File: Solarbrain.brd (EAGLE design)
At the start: 42.9 x 30.4 mm, 51 parts, among them IC1 MCP73871, Q1 MOSFET-NCHANNELSMD, Q2 MOSFET-NCHANNELFDD8580, Q3 MOSFET-NCHANNELSMD, U1 ATMEGA128_SMD

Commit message: fixed a broken connection, clarification on schematic
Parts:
- D1: value (none) -> 1amp
- D3: value (none) -> 3amp
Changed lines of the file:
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@@
 </element>
 <element name="Q2" library="SparkFun2011" package="DPAK" value="MOSFET-NCHANNELFDD8580" x="36.004246875" y="23.721315625" smashed="yes" rot="R270"/>
-<element name="D3" library="SparkFun2011" package="SMA-DIODE" value="" x="8.42645" y="22.02815" smashed="yes" rot="R270">
+<element name="D3" library="SparkFun2011" package="SMA-DIODE" value="3amp" x="8.42645" y="22.02815" smashed="yes" rot="R270">
 <attribute name="NAME" x="10.07745" y="24.31415" size="0.6096" layer="25" rot="R270"/>
 <attribute name="VALUE" x="10.07745" y="21.77415" size="0.4064" layer="27" rot="R270"/>
@@
 <attribute name="VALUE" x="17.937225" y="15.71675625" size="1.27" layer="27" rot="R180"/>
 </element>
-<element name="D1" library="SparkFun2011" package="SMA-DIODE" value="" x="37.4015" y="18.8595" smashed="yes" rot="R180">
+<element name="D1" library="SparkFun2011" package="SMA-DIODE" value="1amp" x="37.4015" y="18.8595" smashed="yes" rot="R180">
 <attribute name="NAME" x="39.6875" y="17.2085" size="0.6096" layer="25" rot="R180"/>
 <attribute name="VALUE" x="37.1475" y="17.2085" size="0.4064" layer="27" rot="R180"/>
@@
 <contactref element="JP3" pad="11"/>
 <contactref element="JP8" pad="5"/>
-<contactref element="JP1" pad="1"/>
 <wire x1="9.271" y1="25.7302" x2="9.478884375" y2="25.7716" width="0.254" layer="1"/>
 <wire x1="8.7214" y1="14.0622" x2="7.80415625" y2="14.0622" width="0.1778" layer="1"/>
@@
 <wire x1="23.845909375" y1="23.951871875" x2="23.82886875" y2="23.68083125" width="0.2032" layer="1"/>
 <wire x1="21.39475" y1="21.397" x2="21.363" y2="23.087" width="0.2032" layer="1"/>
-<wire x1="21.363" y1="23.087" x2="21.2725" y2="23.1775" width="0.2032" layer="1"/>
 <wire x1="18.152228125" y1="15.84325" x2="18.51025" y2="15.875" width="0.2032" layer="1"/>
 <via x="18.51025" y="15.875" extent="1-16" drill="0.8"/>
@@
 <wire x1="26.3525" y1="4.532375" x2="26.360375" y2="4.54025" width="0.6096" layer="1"/>
 <wire x1="26.360375" y1="4.54025" x2="26.416" y2="4.54025" width="0.6096" layer="1"/>
+<contactref element="JP1" pad="1"/>
+<wire x1="21.363" y1="23.087" x2="21.2725" y2="23.087" width="0.4064" layer="1"/>
+<wire x1="21.2725" y1="23.087" x2="21.2725" y2="23.1775" width="0.4064" layer="1"/>
 </signal>
 <signal name="VCC" class="1">

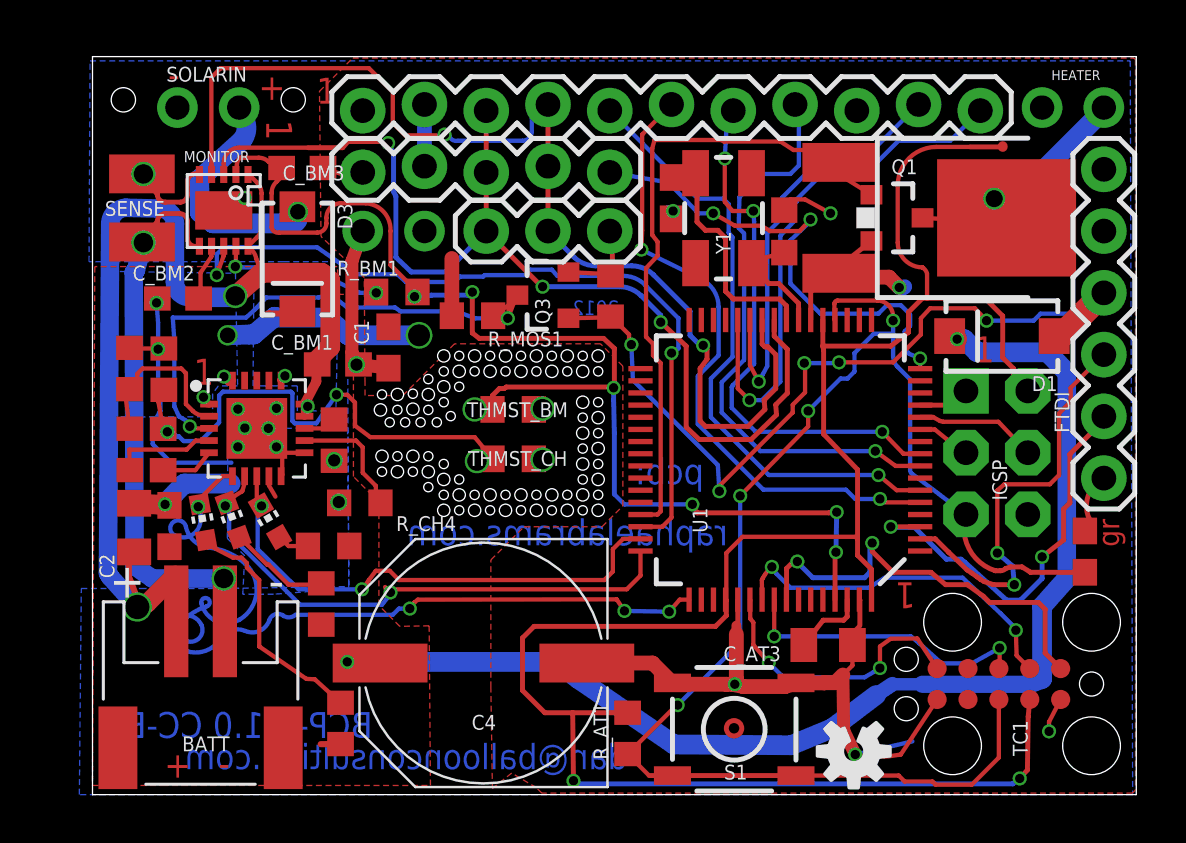
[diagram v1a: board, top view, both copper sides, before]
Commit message: minor tweaks on board, added a via to get to an extra IO pin (pa1)
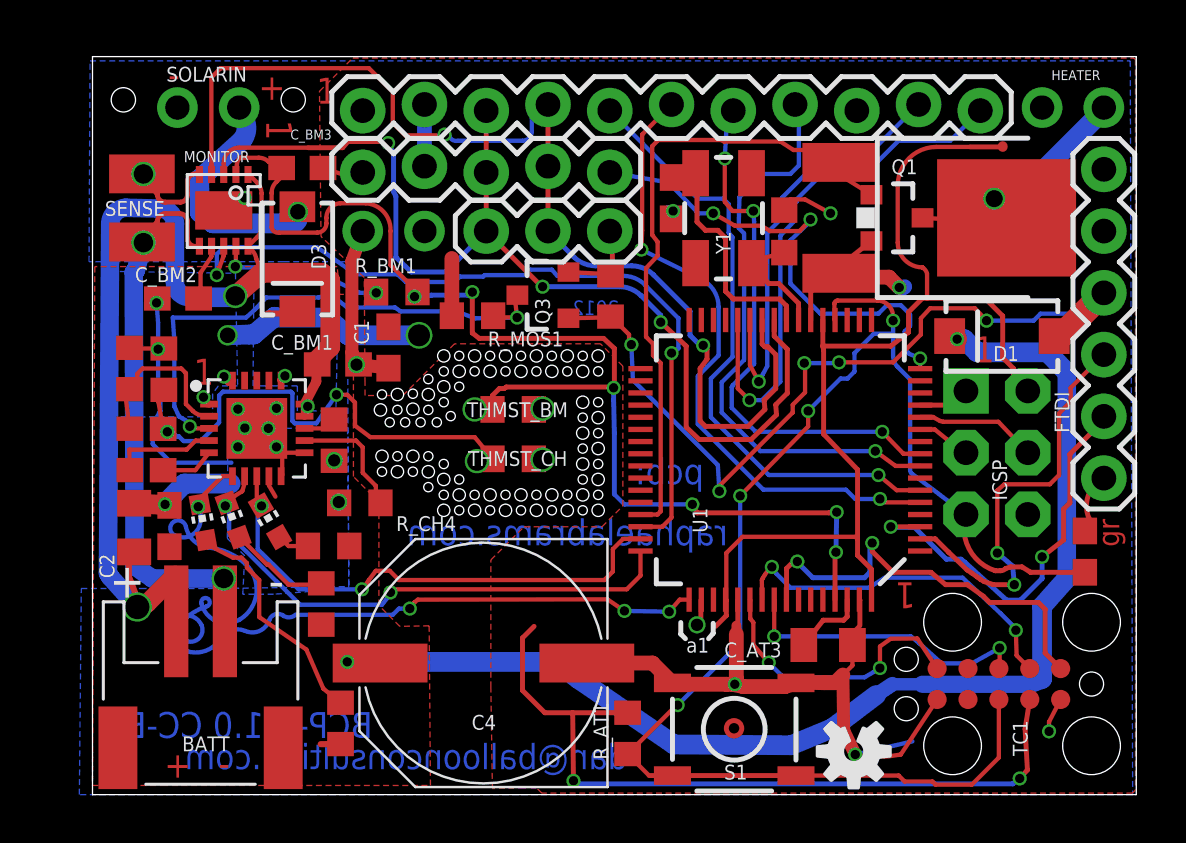
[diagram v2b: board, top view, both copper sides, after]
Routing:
- net 3.3V: track 97.9 -> 90.4 mm
- net N$1: track 0.00 -> 1.03 mm
- net STAT2: track 23.7 -> 23.1 mm
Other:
- board text added: "a1"

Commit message: major tweak list
issues addressed:

  * Atmega Circuit

   1. PWR_EN from sat connector net not connected to any I/O pin on
ATMega

   * Fuel Gauge Circuit

   1. VBATT (BATT) voltage sense trace for the MAX17047 should be a
Kelvin connection - needs to be split and routed separately from the
current carrying portion of trace to a point close to the battery input
   2. CVBATT (C_BM1) should be connected to VBATT's separate kelvin
line and PK-/CSP, not to main current carrying line and GND
   3. CREG (C_BM2) capacitor should be connected to PK-/CSP not GND.
(Figs 5 and 8 data sheet)
   4. THMST_BM should be connected to PK-/CSP- not GND (Fig 5 data
sheet)
   5. PAD should be connected to PK-/CSP not GND

    * JTAG Connector

   1. EAGLE footprint was provided from TC company with incorrect pin
mapping.  Actual numbers should be down-and-up not zig-zag-across.
Need to fix library footprint and re-route traces, for reference, the
TC2050-IDC data sheet is correctly numbered in all views.

    * PCB layout general

   1. All pads in copper pours need thermal cutouts
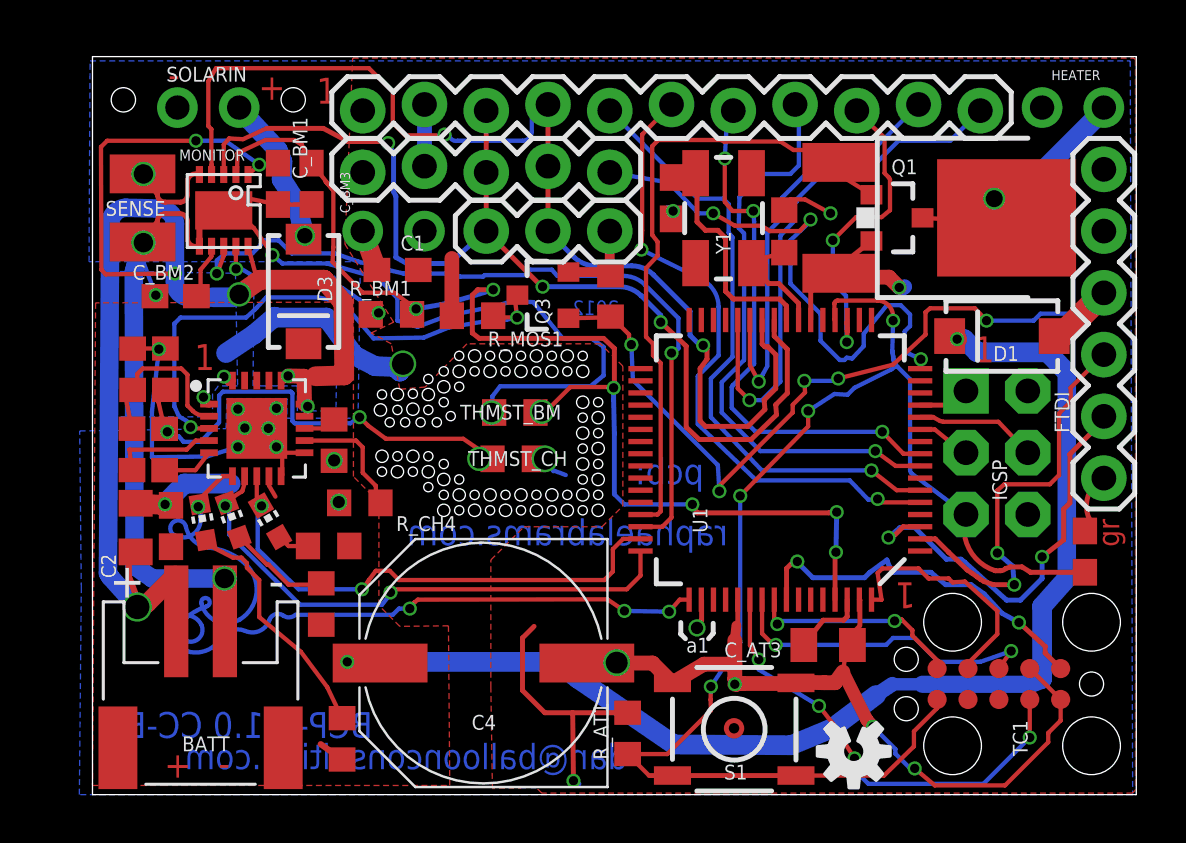
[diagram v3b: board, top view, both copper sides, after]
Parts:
- moved C_BM1 7.82 mm to (7.63, 25.1), turned to 270 degrees
- moved C1 3.21 mm to (12.5, 21.6), turned to 180 degrees
- moved D3 1.36 mm to (8.68, 20.7)
- moved R_BM1 0.95 mm to (12.3, 19.8)
- moved C_BM3 0.75 mm to (9.01, 25.1), turned to 270 degrees
- moved R_LED3 0.64 mm to (10.3, 2.30)
- moved THMST_BM 0.14 mm to (17.4, 15.7), turned to 180 degrees
- moved C_BM2 0.13 mm to (3.42, 20.5)
- moved R_CH2 0.13 mm to (1.65, 17.5)
- moved R_CH1 0.10 mm to (1.62, 14.2)
- moved R_CH6 0.06 mm to (3.00, 17.5)
- moved C2 0.06 mm to (1.78, 11.0)
- moved C3 0.06 mm to (3.23, 11.0)
- moved R_CH5 0.06 mm to (2.97, 14.2)
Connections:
- net CSP: now also C_BM1.2, C_BM2.2, C_BM3.2, MONITOR.P$11, THMST_BM.2
- net GND: no longer C_BM1.2, C_BM2.2, C_BM3.2, MONITOR.P$11, THMST_BM.2
- net PWR_EN: now also U1.19
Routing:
- net 3.3V: track 90.4 -> 35.6 mm, vias 6 -> 4
- net CSP: track 22.9 -> 57.9 mm, vias 2 -> 5
- net BATT: track 47.4 -> 63.1 mm, vias 4 -> 7
- net PWR_EN: track 0.00 -> 13.7 mm, vias 0 -> 2
- net TDI: track 11.8 -> 18.7 mm, vias 2 -> 4
- net GND: track 82.8 -> 76.1 mm, vias 22 -> 19
- net RESET: track 60.7 -> 57.0 mm
- net TMS: track 12.2 -> 8.89 mm
- net N$24: track 9.86 -> 6.73 mm
- net SLEEP: track 20.6 -> 23.3 mm
- net TCK: track 17.6 -> 15.3 mm
- net TDO: track 15.3 -> 13.4 mm
- net THERM_ANALOG: track 50.4 -> 48.7 mm
- net N$8: track 21.6 -> 20.0 mm
- net N$22: track 7.21 -> 8.28 mm
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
